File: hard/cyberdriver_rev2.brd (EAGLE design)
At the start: 59 x 19 mm, 28 parts, among them IC1 OPAMP-DUALU, Q1 MOSFET-NCHANNELBSS123LT1G, U1 ATTINY2313A

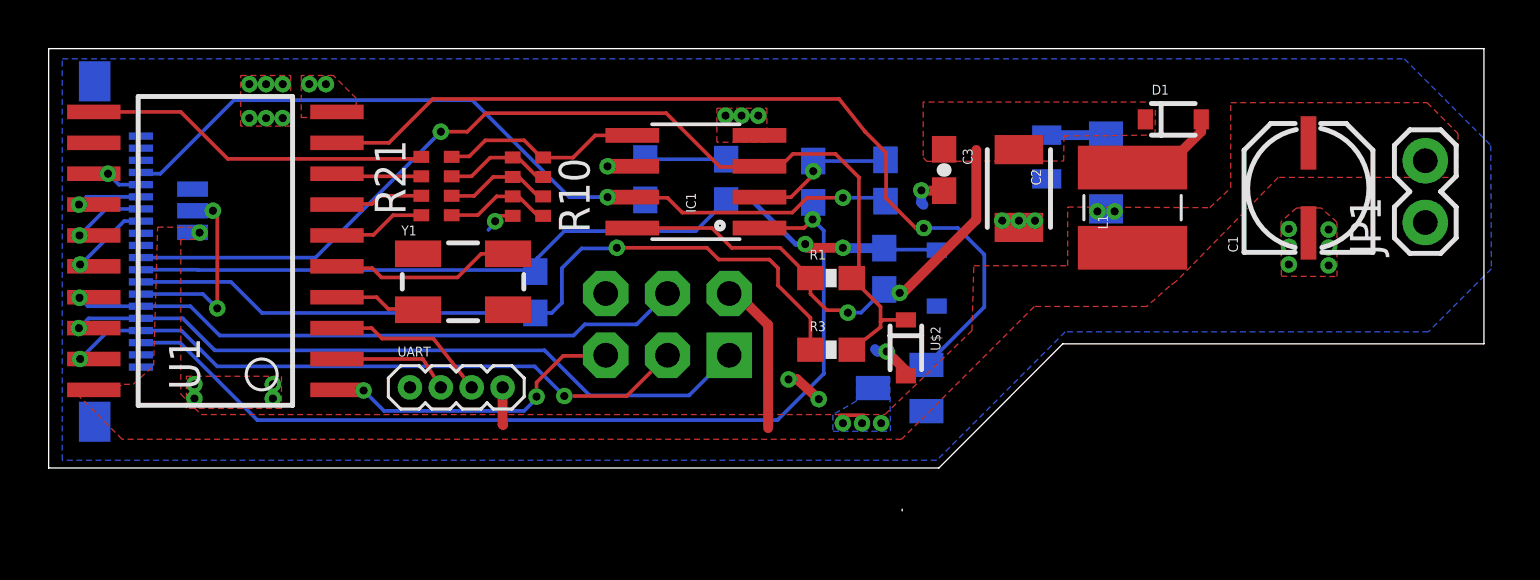
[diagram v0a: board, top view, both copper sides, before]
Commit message: Firmware started (ps working, adc sort of) hardware rev2 started
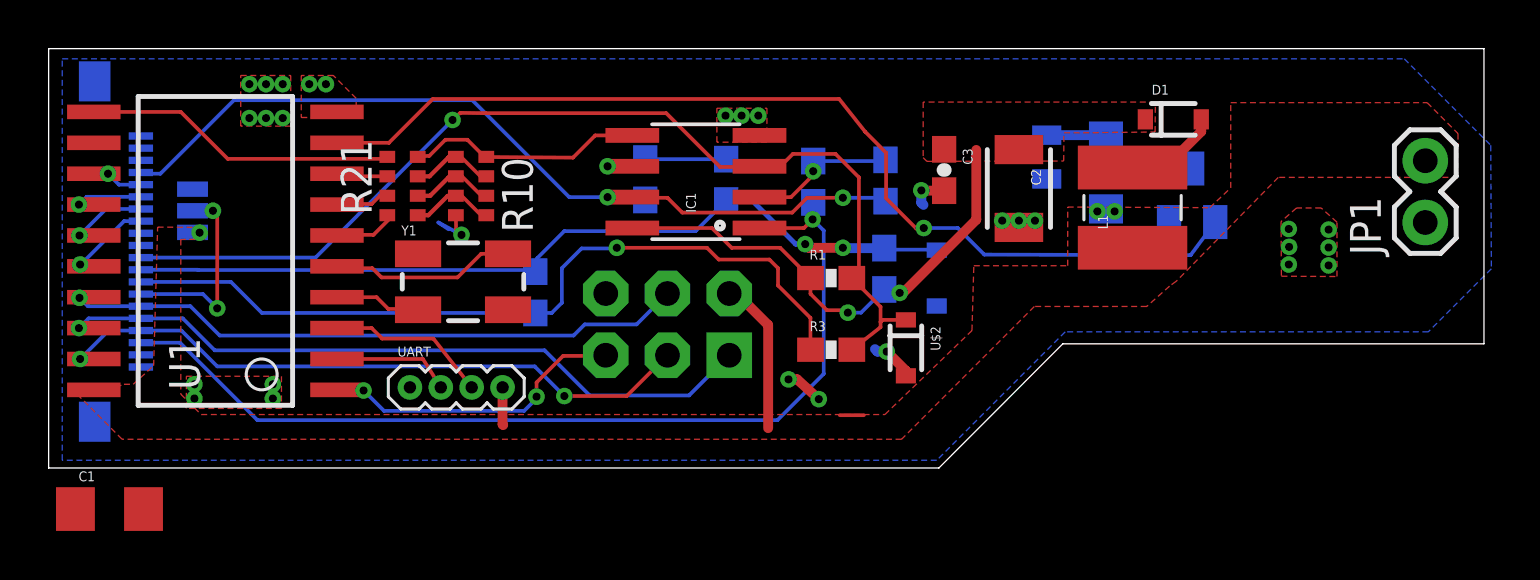
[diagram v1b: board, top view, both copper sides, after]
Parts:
- C1: value 47uF -> (none); device cyberdriver:PANASONIC_C -> SparkFun-Capacitors:1206
- moved C1 50.8 mm to (5.60, 0.08), turned to 0 degrees
- moved Q1 14.4 mm to (50.1, 13.0), turned to 0 degrees
- moved R10 2.34 mm to (20.5, 13.4)
- moved R21 1.40 mm to (17.7, 13.4)
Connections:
- net GND: now also C1.2; no longer C1.-
- net N$4: now also Q1.3
- net VCC: now also C1.1; no longer C1.+, Q1.3
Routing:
- net PS_PWM: track 36.8 -> 41.4 mm
- net AO3: track 14.3 -> 12.9 mm
- net AO2: track 3.51 -> 2.12 mm
- net AO1: track 3.62 -> 2.22 mm
- net A_VID: track 8.38 -> 9.77 mm
- net GND: track 6.75 -> 7.95 mm
- net N$8: track 4.42 -> 3.48 mm
- net N$6: track 4.41 -> 3.48 mm
- net N$9: track 4.41 -> 3.48 mm
- net AO0: track 3.81 -> 2.89 mm
- net VCC: vias 6 -> 3
- removed copper zone on layer 16, net VCC
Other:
- board size 59 x 19 mm -> 59 x 17.2 mm
